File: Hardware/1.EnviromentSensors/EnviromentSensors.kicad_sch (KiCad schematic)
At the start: 14 parts, among them J2 Conn_01x05_Pin, U1 SHT4x, U2 BME680, U3 LPS22HB

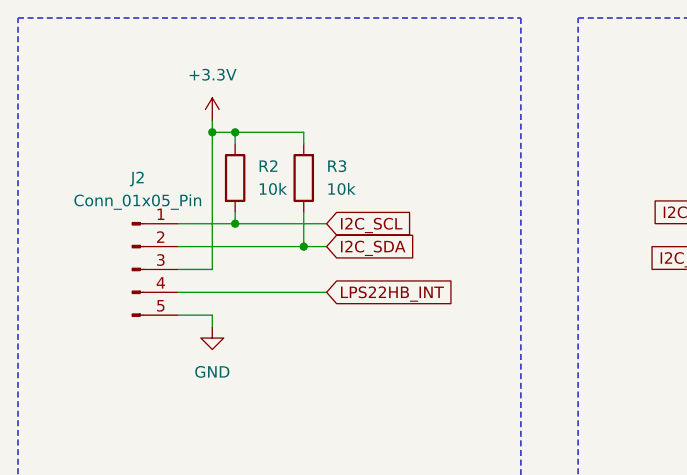
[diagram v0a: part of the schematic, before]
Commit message: Change pullup resistor from 10k to 4.7k
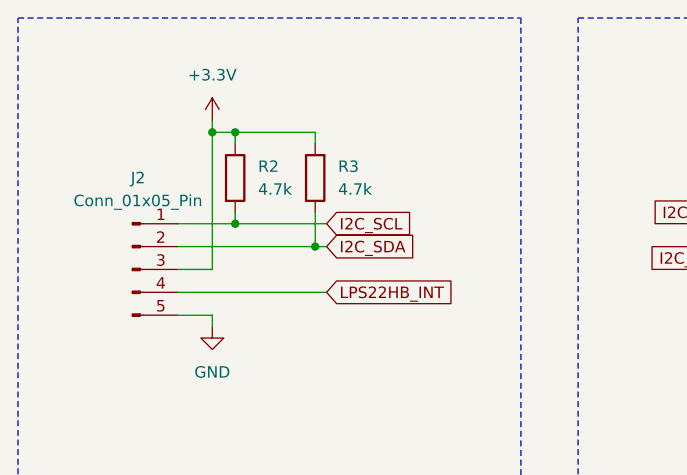
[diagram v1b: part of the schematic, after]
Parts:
- R2, R3: value 10k -> 4.7k
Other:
- moved on the sheet: R3
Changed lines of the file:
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@@
   (junction (at 238.76 111.76) (diameter 0) (color 0 0 0 0)
   )
+  (junction (at 52.07 44.45) (diameter 0) (color 0 0 0 0)
+  )
   (junction (at 205.74 64.77) (diameter 0) (color 0 0 0 0)
   )
@@
   (junction (at 200.66 128.27) (diameter 0) (color 0 0 0 0)
   )
-  (junction (at 50.8 44.45) (diameter 0) (color 0 0 0 0)
-  )
   (junction (at 43.18 31.75) (diameter 0) (color 0 0 0 0)
   )
@@
     (stroke (width 0) (type default))
   )
-  (wire (pts (xy 50.8 44.45) (xy 53.34 44.45))
-    (stroke (width 0) (type default))
-  )
   (wire (pts (xy 218.44 102.87) (xy 201.93 102.87))
     (stroke (width 0) (type default))
@@
     (stroke (width 0) (type default))
   )
-  (wire (pts (xy 50.8 40.64) (xy 50.8 44.45))
+  (wire (pts (xy 52.07 40.64) (xy 52.07 44.45))
     (stroke (width 0) (type default))
   )
@@
     (stroke (width 0) (type default))
   )
+  (wire (pts (xy 52.07 44.45) (xy 53.34 44.45))
+    (stroke (width 0) (type default))
+  )
   (wire (pts (xy 173.99 31.75) (xy 185.42 31.75))
     (stroke (width 0) (type default))
@@
     (stroke (width 0) (type default))
   )
-  (wire (pts (xy 36.83 44.45) (xy 50.8 44.45))
+  (wire (pts (xy 36.83 44.45) (xy 52.07 44.45))
     (stroke (width 0) (type default))
   )
@@
     (stroke (width 0) (type default))
   )
-  (wire (pts (xy 43.18 31.75) (xy 50.8 31.75))
+  (wire (pts (xy 43.18 31.75) (xy 52.07 31.75))
     (stroke (width 0) (type default))
   )
@@
     (stroke (width 0) (type default))
   )
-  (wire (pts (xy 50.8 31.75) (xy 50.8 33.02))
+  (wire (pts (xy 52.07 31.75) (xy 52.07 33.02))
     (stroke (width 0) (type default))
   )
@@
     )
   )
-  (symbol (lib_id "Device:R") (at 50.8 36.83 180) (unit 1)
-    (in_bom yes) (on_board yes) (dnp no) (fields_autoplaced)
-    (property "Reference" "R3" (at 53.34 35.56 0)
+  (symbol (lib_id "Device:R") (at 52.07 36.83 180) (unit 1)
+    (in_bom yes) (on_board yes) (dnp no) (fields_autoplaced)
+    (property "Reference" "R3" (at 54.61 35.56 0)
       (effects (font (size 1.27 1.27)) (justify right))
     )
-    (property "Value" "10k" (at 53.34 38.1 0)
+    (property "Value" "4.7k" (at 54.61 38.1 0)
       (effects (font (size 1.27 1.27)) (justify right))
     )
-    (property "Footprint" "" (at 52.578 36.83 90)
-      (effects (font (size 1.27 1.27)) hide)
-    )
-    (property "Datasheet" "~" (at 50.8 36.83 0)
+    (property "Footprint" "" (at 53.848 36.83 90)
+      (effects (font (size 1.27 1.27)) hide)
+    )
+    (property "Datasheet" "~" (at 52.07 36.83 0)
       (effects (font (size 1.27 1.27)) hide)
     )
@@
       (effects (font (size 1.27 1.27)) (justify left))
     )
-    (property "Value" "10k" (at 45.72 38.1 0)
+    (property "Value" "4.7k" (at 45.72 38.1 0)
       (effects (font (size 1.27 1.27)) (justify left))
     )

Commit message: Fill revision and schematic date fields
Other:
- title: (none) -> Enviroment Sensors
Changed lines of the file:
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@@
 (kicad_sch (version 20230121) (generator eeschema)
   (paper "A4")
+  (title_block
+    (title "Enviroment Sensors")
+    (date "2023-07-17")
+    (rev "A")
+  )
   (junction (at 203.2 31.75) (diameter 0) (color 0 0 0 0)
   )

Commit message: Add Power flag to solve ECR errors
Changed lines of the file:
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@@
+    (stroke (width 0) (type default))
+  )
+  (wire (pts (xy 59.69 72.39) (xy 59.69 74.93))
     (stroke (width 0) (type default))
   )
@@
   )
   (wire (pts (xy 167.64 102.87) (xy 180.34 102.87))
+    (stroke (width 0) (type default))
+  )
+  (wire (pts (xy 68.58 74.93) (xy 68.58 72.39))
     (stroke (width 0) (type default))
   )
@@
     )
   )
+  (symbol (lib_id "power:PWR_FLAG") (at 68.58 72.39 0) (unit 1)
+    (in_bom yes) (on_board yes) (dnp no) (fields_autoplaced)
+    (property "Reference" "#FLG02" (at 68.58 70.485 0)
+      (effects (font (size 1.27 1.27)) hide)
+    )
+    (property "Value" "PWR_FLAG" (at 68.58 67.31 0)
+      (effects (font (size 1.27 1.27)))
+    )
+    (property "Footprint" "" (at 68.58 72.39 0)
+      (effects (font (size 1.27 1.27)) hide)
+    )
+    (property "Datasheet" "~" (at 68.58 72.39 0)
+      (effects (font (size 1.27 1.27)) hide)
+    )
+    (pin "1")
+    (instances
+      (project "EnviromentSensors"
+        (path "/fc1a0c50-39ba-4cf6-ad6f-af313c028135"
+          (reference "#FLG02") (unit 1)
+        )
+      )
+    )
+  )
   (symbol (lib_id "Device:C") (at 173.99 36.83 0) (unit 1)
     (in_bom yes) (on_board yes) (dnp no)
@@
     )
   )
+  (symbol (lib_id "power:PWR_FLAG") (at 59.69 74.93 180) (unit 1)
+    (in_bom yes) (on_board yes) (dnp no) (fields_autoplaced)
+    (property "Reference" "#FLG01" (at 59.69 76.835 0)
+      (effects (font (size 1.27 1.27)) hide)
+    )
+    (property "Value" "PWR_FLAG" (at 59.69 80.01 0)
+      (effects (font (size 1.27 1.27)))
+    )
+    (property "Footprint" "" (at 59.69 74.93 0)
+      (effects (font (size 1.27 1.27)) hide)
+    )
+    (property "Datasheet" "~" (at 59.69 74.93 0)
+      (effects (font (size 1.27 1.27)) hide)
+    )
+    (pin "1")
+    (instances
+      (project "EnviromentSensors"
+        (path "/fc1a0c50-39ba-4cf6-ad6f-af313c028135"
+          (reference "#FLG01") (unit 1)
+        )
+      )
+    )
+  )
   (symbol (lib_id "Connector:Conn_01x05_Pin") (at 31.75 46.99 0) (unit 1)
     (in_bom yes) (on_board yes) (dnp no) (fields_autoplaced)
@@
         (path "/fc1a0c50-39ba-4cf6-ad6f-af313c028135"
           (reference "#PWR04") (unit 1)
+        )
+      )
+    )
+  )
+  (symbol (lib_id "power:+3.3V") (at 59.69 72.39 0) (unit 1)
+    (in_bom yes) (on_board yes) (dnp no) (fields_autoplaced)
+    (property "Reference" "#PWR015" (at 59.69 76.2 0)
+      (effects (font (size 1.27 1.27)) hide)
+    )
+    (property "Value" "+3.3V" (at 59.69 67.31 0)
+      (effects (font (size 1.27 1.27)))
+    )
+    (property "Footprint" "" (at 59.69 72.39 0)
+      (effects (font (size 1.27 1.27)) hide)
+    )
+    (property "Datasheet" "" (at 59.69 72.39 0)
+      (effects (font (size 1.27 1.27)) hide)
+    )
+    (pin "1")
+    (instances
+      (project "EnviromentSensors"
+        (path "/fc1a0c50-39ba-4cf6-ad6f-af313c028135"
+          (reference "#PWR015") (unit 1)
         )
       )
@@
         )
       )
+    )
+  )
+  (symbol (lib_id "power:GND") (at 68.58 74.93 0) (unit 1)
+    (in_bom yes) (on_board yes) (dnp no) (fields_autoplaced)
+    (property "Reference" "#PWR016" (at 68.58 81.28 0)
+      (effects (font (size 1.27 1.27)) hide)
+    )
+    (property "Value" "GND" (at 68.58 80.01 0)
+      (effects (font (size 1.27 1.27)))
+    )
+    (property "Footprint" "" (at 68.58 74.93 0)
+      (effects (font (size 1.27 1.27)) hide)
+    )
+    (property "Datasheet" "" (at 68.58 74.93 0)
+      (effects (font (size 1.27 1.27)) hide)
+    )
+    (pin "1")
+    (instances
+      (project "EnviromentSensors"
+        (path "/fc1a0c50-39ba-4cf6-ad6f-af313c028135"
+          (reference "#PWR016") (unit 1)
+        )
+      )

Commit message: Assign footprint for schematic elements
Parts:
- C1, C2, C3, C4: footprint (none) -> Capacitor_SMD:C_0201_0603Metric_Pad0.64x0.40mm_HandSolder
- J2: footprint (none) -> Connector_JST:JST_PH_S5B-PH-K_1x05_P2.00mm_Horizontal
- JP1, JP2: footprint (none) -> Jumper:SolderJumper-2_P1.3mm_Open_TrianglePad1.0x1.5mm
- R1, R2, R3, R4: footprint (none) -> Resistor_SMD:R_0201_0603Metric_Pad0.64x0.40mm_HandSolder
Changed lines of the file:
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@@
       (effects (font (size 1.27 1.27)) (justify right) hide)
     )
-    (property "Footprint" "" (at 238.76 45.72 0)
+    (property "Footprint" "Jumper:SolderJumper-2_P1.3mm_Open_TrianglePad1.0x1.5mm" (at 238.76 45.72 0)
       (effects (font (size 1.27 1.27)) hide)
     )
@@
       (effects (font (size 1.27 1.27)) (justify left))
     )
-    (property "Footprint" "" (at 174.9552 40.64 0)
+    (property "Footprint" "Capacitor_SMD:C_0201_0603Metric_Pad0.64x0.40mm_HandSolder" (at 174.9552 40.64 0)
       (effects (font (size 1.27 1.27)) hide)
     )
@@
       (effects (font (size 1.27 1.27)))
     )
-    (property "Footprint" "" (at 31.75 46.99 0)
+    (property "Footprint" "Connector_JST:JST_PH_S5B-PH-K_1x05_P2.00mm_Horizontal" (at 31.75 46.99 0)
       (effects (font (size 1.27 1.27)) hide)
     )
@@
       (effects (font (size 1.27 1.27)) (justify right))
     )
-    (property "Footprint" "" (at 53.848 36.83 90)
+    (property "Footprint" "Resistor_SMD:R_0201_0603Metric_Pad0.64x0.40mm_HandSolder" (at 53.848 36.83 90)
       (effects (font (size 1.27 1.27)) hide)
     )
@@
       (effects (font (size 1.27 1.27)) (justify left))
     )
-    (property "Footprint" "" (at 41.402 36.83 90)
+    (property "Footprint" "Resistor_SMD:R_0201_0603Metric_Pad0.64x0.40mm_HandSolder" (at 41.402 36.83 90)
       (effects (font (size 1.27 1.27)) hide)
     )
@@
       (effects (font (size 1.27 1.27)) (justify left))
     )
-    (property "Footprint" "" (at 236.982 35.56 90)
+    (property "Footprint" "Resistor_SMD:R_0201_0603Metric_Pad0.64x0.40mm_HandSolder" (at 236.982 35.56 90)
       (effects (font (size 1.27 1.27)) hide)
     )
@@
       (effects (font (size 1.27 1.27)) (justify left))
     )
-    (property "Footprint" "" (at 186.3852 40.64 0)
+    (property "Footprint" "Capacitor_SMD:C_0201_0603Metric_Pad0.64x0.40mm_HandSolder" (at 186.3852 40.64 0)
       (effects (font (size 1.27 1.27)) hide)
     )
@@
       (effects (font (size 1.27 1.27)) (justify left))
     )
-    (property "Footprint" "" (at 236.982 106.68 90)
+    (property "Footprint" "Resistor_SMD:R_0201_0603Metric_Pad0.64x0.40mm_HandSolder" (at 236.982 106.68 90)
       (effects (font (size 1.27 1.27)) hide)
     )
@@
       (effects (font (size 1.27 1.27)) (justify left))
     )
-    (property "Footprint" "" (at 168.6052 111.76 0)
+    (property "Footprint" "Capacitor_SMD:C_0201_0603Metric_Pad0.64x0.40mm_HandSolder" (at 168.6052 111.76 0)
       (effects (font (size 1.27 1.27)) hide)
     )
@@
       (effects (font (size 1.27 1.27)) (justify right) hide)
     )
-    (property "Footprint" "" (at 238.76 116.84 0)
+    (property "Footprint" "Jumper:SolderJumper-2_P1.3mm_Open_TrianglePad1.0x1.5mm" (at 238.76 116.84 0)
       (effects (font (size 1.27 1.27)) hide)
     )
@@
       (effects (font (size 1.27 1.27)) (justify left))
     )
-    (property "Footprint" "" (at 181.3052 111.76 0)
-      (effects (font (size 1.27 1.27)) hide)
-    )
+    (property "Footprint" "Capacitor_SMD:C_0201_0603Metric_Pad0.64x0.40mm_HandSolder" (at 181.3052 111.76 0)
+      (effects (font (size 1.27 1.27)) hide)
+    )

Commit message: Change resistors and capasitors footprint from 0201 to 0402
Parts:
- C1, C2, C3, C4: footprint Capacitor_SMD:C_0201_0603Metric_Pad0.64x0.40mm_HandSolder -> Capacitor_SMD:C_0402_1005Metric
- R1, R2, R3, R4: footprint Resistor_SMD:R_0201_0603Metric_Pad0.64x0.40mm_HandSolder -> Resistor_SMD:R_0402_1005Metric
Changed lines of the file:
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@@
       (effects (font (size 1.27 1.27)) (justify left))
     )
-    (property "Footprint" "Capacitor_SMD:C_0201_0603Metric_Pad0.64x0.40mm_HandSolder" (at 174.9552 40.64 0)
+    (property "Footprint" "Capacitor_SMD:C_0402_1005Metric" (at 174.9552 40.64 0)
       (effects (font (size 1.27 1.27)) hide)
     )
@@
       (effects (font (size 1.27 1.27)) (justify right))
     )
-    (property "Footprint" "Resistor_SMD:R_0201_0603Metric_Pad0.64x0.40mm_HandSolder" (at 53.848 36.83 90)
+    (property "Footprint" "Resistor_SMD:R_0402_1005Metric" (at 53.848 36.83 90)
       (effects (font (size 1.27 1.27)) hide)
     )
@@
       (effects (font (size 1.27 1.27)) (justify left))
     )
-    (property "Footprint" "Resistor_SMD:R_0201_0603Metric_Pad0.64x0.40mm_HandSolder" (at 41.402 36.83 90)
+    (property "Footprint" "Resistor_SMD:R_0402_1005Metric" (at 41.402 36.83 90)
       (effects (font (size 1.27 1.27)) hide)
     )
@@
       (effects (font (size 1.27 1.27)) (justify left))
     )
-    (property "Footprint" "Resistor_SMD:R_0201_0603Metric_Pad0.64x0.40mm_HandSolder" (at 236.982 35.56 90)
+    (property "Footprint" "Resistor_SMD:R_0402_1005Metric" (at 236.982 35.56 90)
       (effects (font (size 1.27 1.27)) hide)
     )
@@
       (effects (font (size 1.27 1.27)) (justify left))
     )
-    (property "Footprint" "Capacitor_SMD:C_0201_0603Metric_Pad0.64x0.40mm_HandSolder" (at 186.3852 40.64 0)
+    (property "Footprint" "Capacitor_SMD:C_0402_1005Metric" (at 186.3852 40.64 0)
       (effects (font (size 1.27 1.27)) hide)
     )
@@
       (effects (font (size 1.27 1.27)) (justify left))
     )
-    (property "Footprint" "Resistor_SMD:R_0201_0603Metric_Pad0.64x0.40mm_HandSolder" (at 236.982 106.68 90)
+    (property "Footprint" "Resistor_SMD:R_0402_1005Metric" (at 236.982 106.68 90)
       (effects (font (size 1.27 1.27)) hide)
     )
@@
       (effects (font (size 1.27 1.27)) (justify left))
     )
-    (property "Footprint" "Capacitor_SMD:C_0201_0603Metric_Pad0.64x0.40mm_HandSolder" (at 168.6052 111.76 0)
+    (property "Footprint" "Capacitor_SMD:C_0402_1005Metric" (at 168.6052 111.76 0)
       (effects (font (size 1.27 1.27)) hide)
     )
@@
       (effects (font (size 1.27 1.27)) (justify left))
     )
-    (property "Footprint" "Capacitor_SMD:C_0201_0603Metric_Pad0.64x0.40mm_HandSolder" (at 181.3052 111.76 0)
-      (effects (font (size 1.27 1.27)) hide)
-    )
+    (property "Footprint" "Capacitor_SMD:C_0402_1005Metric" (at 181.3052 111.76 0)
+      (effects (font (size 1.27 1.27)) hide)
+    )

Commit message: Add LCSC part numbers for electronic components
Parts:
- C1, C2, C3: MPN (none) -> C77020
- C4: MPN (none) -> C2858031
- JP1, JP2: now left out of the parts list
- R1, R4: MPN (none) -> C25744
- R2, R3: MPN (none) -> C25940
- U2: MPN (none) -> C125972
- U3: MPN (none) -> C94049
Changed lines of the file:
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@@
   )
   (symbol (lib_id "Jumper:SolderJumper_2_Open") (at 238.76 45.72 90) (unit 1)
-    (in_bom yes) (on_board yes) (dnp no) (fields_autoplaced)
+    (in_bom no) (on_board yes) (dnp no) (fields_autoplaced)
     (property "Reference" "JP1" (at 241.3 44.45 90)
       (effects (font (size 1.27 1.27)) (justify right))
@@
     )
     (property "Datasheet" "~" (at 238.76 45.72 0)
+      (effects (font (size 1.27 1.27)) hide)
+    )
+    (property "MPN" "" (at 238.76 45.72 0)
       (effects (font (size 1.27 1.27)) hide)
     )
@@
       (effects (font (size 1.27 1.27)) hide)
     )
+    (property "MPN" "	C77020" (at 173.99 36.83 0)
+      (effects (font (size 1.27 1.27)) hide)
+    )
     (pin "1")
     (pin "2")
@@
     )
     (property "Datasheet" "~" (at 31.75 46.99 0)
+      (effects (font (size 1.27 1.27)) hide)
+    )
+    (property "MPN" "" (at 31.75 46.99 0)
       (effects (font (size 1.27 1.27)) hide)
     )
@@
       (effects (font (size 1.27 1.27)) hide)
     )
+    (property "MPN" "C25940" (at 52.07 36.83 0)
+      (effects (font (size 1.27 1.27)) hide)
+    )
     (pin "1")
     (pin "2")
@@
     )
     (property "Datasheet" "~" (at 43.18 36.83 0)
+      (effects (font (size 1.27 1.27)) hide)
+    )
+    (property "MPN" "C25940" (at 43.18 36.83 0)
       (effects (font (size 1.27 1.27)) hide)
     )
@@
     (property "Datasheet" "https://www.st.com/resource/en/datasheet/lps22hb.pdf" (at 205.74 130.81 0)
       (effects (font (size 1.27 1.27)) (justify left) hide)
+    )
+    (property "MPN" "C94049" (at 204.47 116.84 0)
+      (effects (font (size 1.27 1.27)) hide)
     )
     (pin "1")
@@
       (effects (font (size 1.27 1.27)) hide)
     )
+    (property "MPN" "C25744" (at 238.76 35.56 0)
+      (effects (font (size 1.27 1.27)) hide)
+    )
     (pin "1")
     (pin "2")
@@
     )
     (property "Datasheet" "~" (at 185.42 36.83 0)
+      (effects (font (size 1.27 1.27)) hide)
+    )
+    (property "MPN" "	C77020" (at 185.42 36.83 0)
       (effects (font (size 1.27 1.27)) hide)
     )
@@
     )
     (property "Datasheet" "https://ae-bst.resource.bosch.com/media/_tech/media/datasheets/BST-BME680-DS001.pdf" (at 205.74 53.34 0)
+      (effects (font (size 1.27 1.27)) hide)
+    )
+    (property "MPN" "C125972" (at 205.74 48.26 0)
       (effects (font (size 1.27 1.27)) hide)
     )
@@
       (effects (font (size 1.27 1.27)) hide)
     )
+    (property "MPN" "C25744" (at 238.76 106.68 0)
+      (effects (font (size 1.27 1.27)) hide)
+    )
     (pin "1")
     (pin "2")
@@
       (effects (font (size 1.27 1.27)) hide)
     )
+    (property "MPN" "C2858031" (at 167.64 107.95 0)
+      (effects (font (size 1.27 1.27)) hide)
+    )
     (pin "1")
     (pin "2")
@@
   )
   (symbol (lib_id "Jumper:SolderJumper_2_Open") (at 238.76 116.84 90) (unit 1)
-    (in_bom yes) (on_board yes) (dnp no) (fields_autoplaced)
+    (in_bom no) (on_board yes) (dnp no) (fields_autoplaced)
     (property "Reference" "JP2" (at 241.3 115.57 90)
       (effects (font (size 1.27 1.27)) (justify right))
@@
       (effects (font (size 1.27 1.27)) hide)
     )
+    (property "MPN" "" (at 238.76 116.84 0)
+      (effects (font (size 1.27 1.27)) hide)
+    )
     (pin "1")
     (pin "2")
@@
     )
     (property "Datasheet" "~" (at 180.34 107.95 0)
+      (effects (font (size 1.27 1.27)) hide)
+    )
+    (property "MPN" "	C77020" (at 180.34 107.95 0)
       (effects (font (size 1.27 1.27)) hide)
     )
@@
       (effects (font (size 1.27 1.27)) (justify left) hide)
     )
-    (pin "1")
+    (property "MPN" "" (at 110.49 43.18 0)
+      (effects (font (size 1.27 1.27)) hide)
+    )
+    (pin "1")
